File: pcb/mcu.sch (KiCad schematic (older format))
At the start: 24 parts, among them J1 Conn_01x04_Male, J2 Conn_01x04_Male, J3 Conn_01x03_Male, J4 Conn_01x03_Male, SW1 SW_Push, U1 STM32F103C8Tx, Y1 32.768KHz, Y2 8MHz

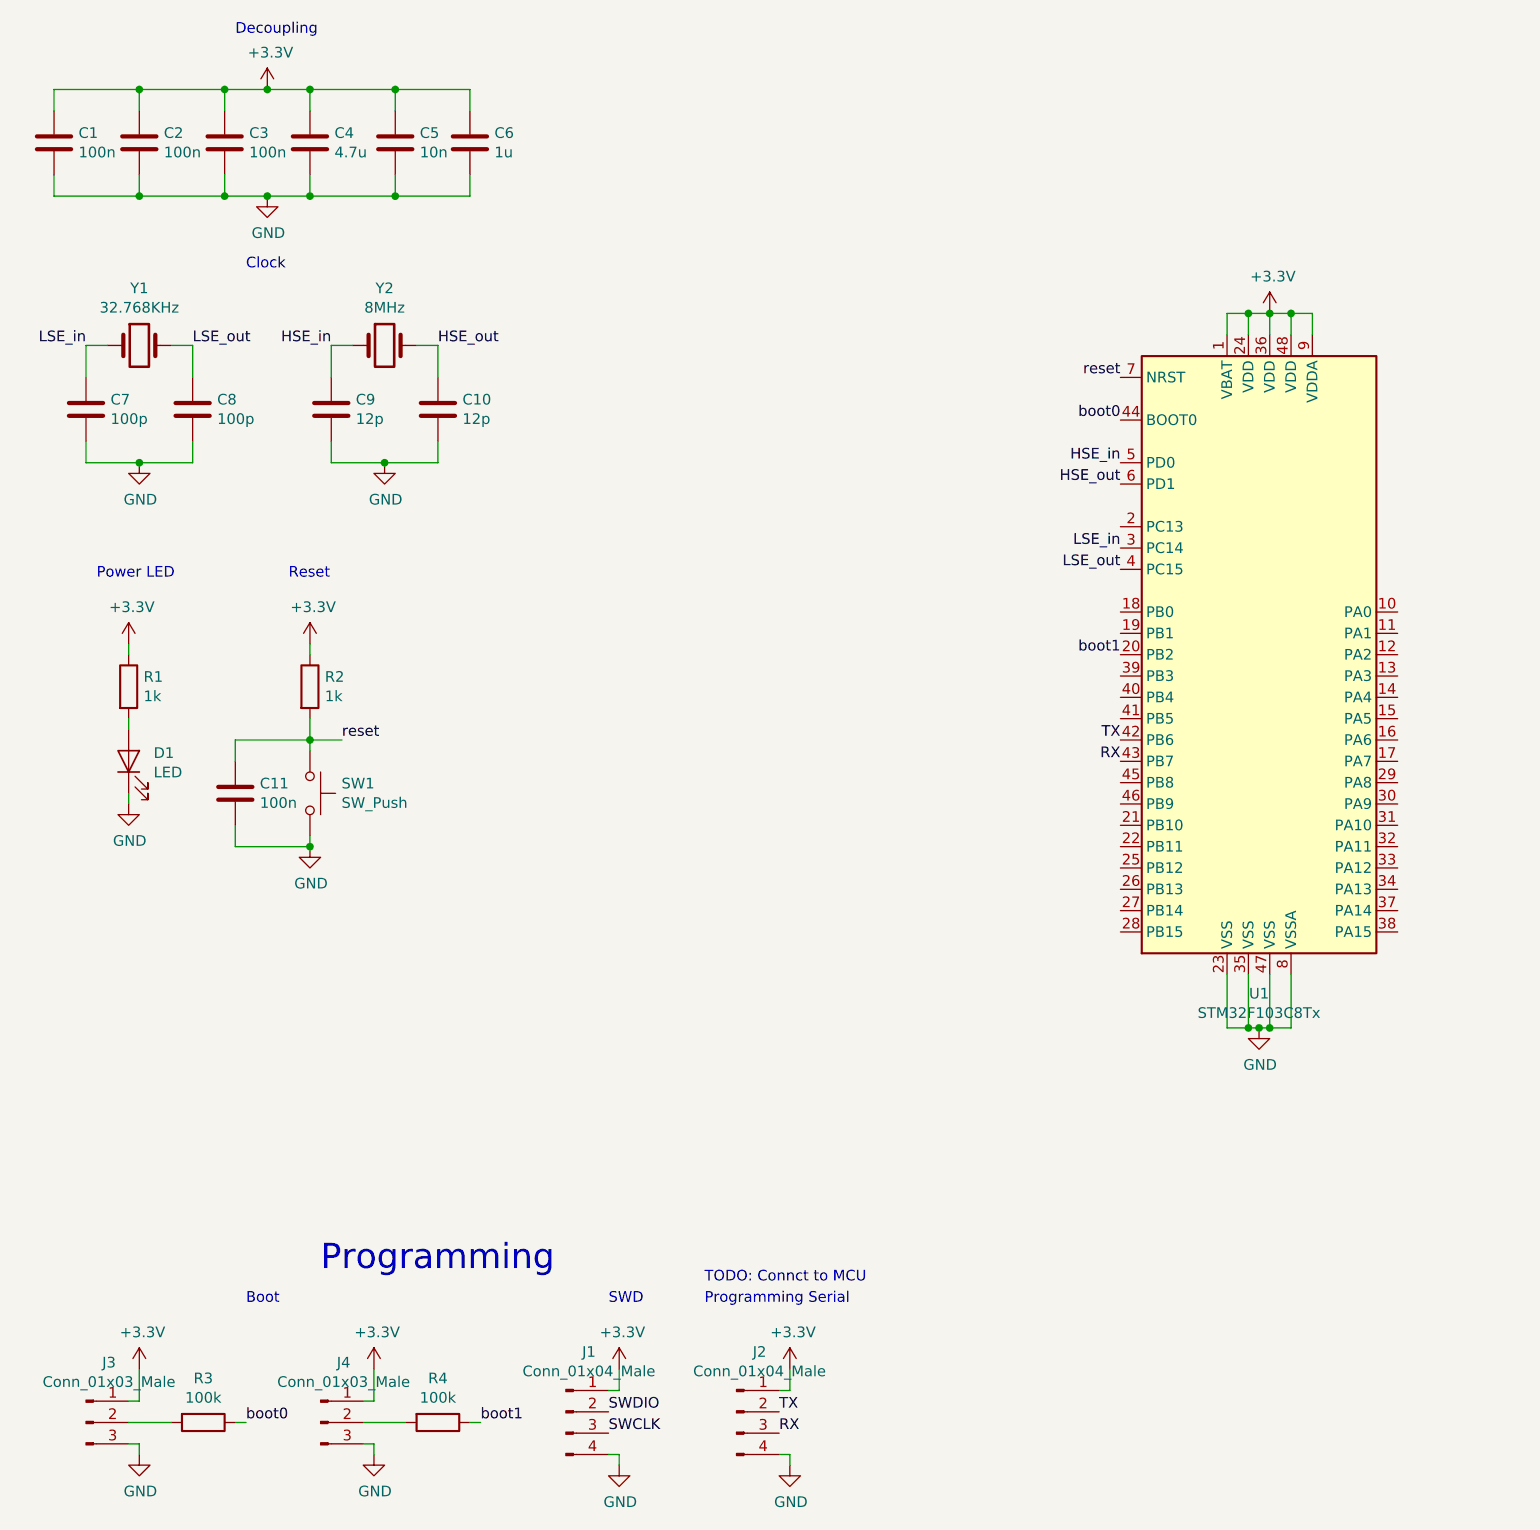
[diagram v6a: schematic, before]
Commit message: Use Buses for IR sensors
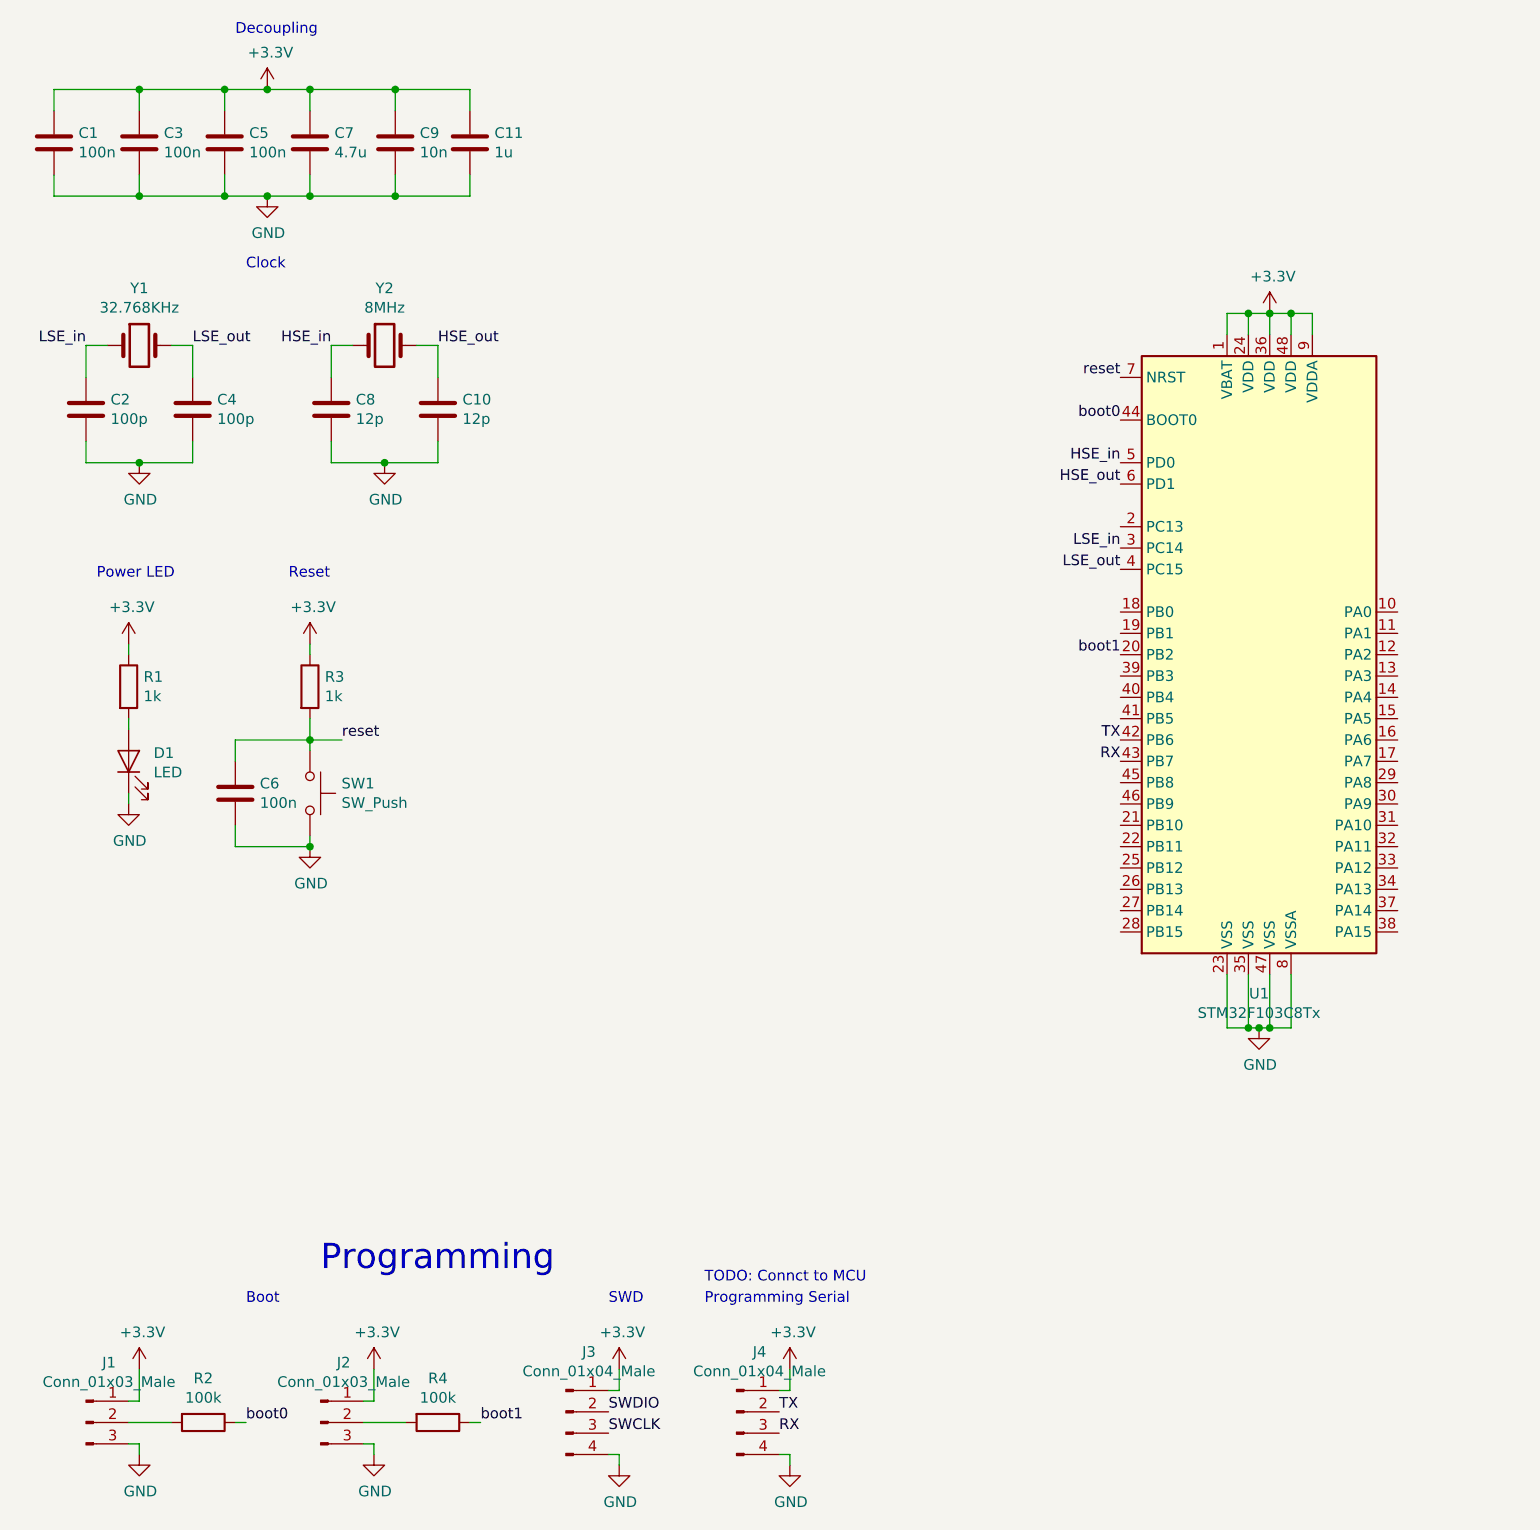
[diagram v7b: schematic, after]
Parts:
- renumbered C6 to C11, C7 to C2, C2 to C3, C8 to C4, C3 to C5, C11 to C6, C4 to C7, C9 to C8, C5 to C9, J3 to J1, J4 to J2, J1 to J3, J2 to J4, R3 to R2, R2 to R3
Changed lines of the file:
@@
 $Descr A4 11693 8268
 encoding utf-8
-Sheet 2 17
+Sheet 2 19
 Title ""
 Date ""
@@
 $EndComp
 $Comp
-L power:GND #PWR010
+L power:GND #PWR017
 U 1 1 5D0B3E48
 P 6300 5250
-F 0 "#PWR010" H 6300 5000 50  0001 C CNN
+F 0 "#PWR017" H 6300 5000 50  0001 C CNN
 F 1 "GND" H 6305 5077 50  0000 C CNN
 F 2 "" H 6300 5250 50  0001 C CNN
@@
 Decoupling
 $Comp
-L power:+3.3V #PWR01
+L power:+3.3V #PWR06
 U 1 1 5D0BC77C
 P 1650 850
-F 0 "#PWR01" H 1650 700 50  0001 C CNN
+F 0 "#PWR06" H 1650 700 50  0001 C CNN
 F 1 "+3.3V" H 1665 1023 50  0000 C CNN
 F 2 "" H 1650 850 50  0001 C CNN
@@
 $EndComp
 $Comp
-L Device:C C2
+L Device:C C3
 U 1 1 5D0BD12F
 P 1050 1100
-F 0 "C2" H 1165 1146 50  0000 L CNN
+F 0 "C3" H 1165 1146 50  0000 L CNN
 F 1 "100n" H 1165 1055 50  0000 L CNN
 F 2 "Capacitor_SMD:C_0805_2012Metric" H 1088 950 50  0001 C CNN
@@
 $EndComp
 $Comp
-L Device:C C3
+L Device:C C5
 U 1 1 5D0BD74C
 P 1450 1100
-F 0 "C3" H 1565 1146 50  0000 L CNN
+F 0 "C5" H 1565 1146 50  0000 L CNN
 F 1 "100n" H 1565 1055 50  0000 L CNN
 F 2 "Capacitor_SMD:C_0805_2012Metric" H 1488 950 50  0001 C CNN
@@
 	6350 1900 6250 1900
 $Comp
-L power:+3.3V #PWR03
+L power:+3.3V #PWR018
 U 1 1 5D0AFF21
 P 6350 1900
-F 0 "#PWR03" H 6350 1750 50  0001 C CNN
+F 0 "#PWR018" H 6350 1750 50  0001 C CNN
 F 1 "+3.3V" H 6365 2073 50  0000 C CNN
 F 2 "" H 6350 1900 50  0001 C CNN
@@
 	6300 5250 6250 5250
 $Comp
-L Device:C C4
+L Device:C C7
 U 1 1 5D0C6E4D
 P 1850 1100
-F 0 "C4" H 1965 1146 50  0000 L CNN
+F 0 "C7" H 1965 1146 50  0000 L CNN
 F 1 "4.7u" H 1965 1055 50  0000 L CNN
 F 2 "Capacitor_SMD:C_0805_2012Metric" H 1888 950 50  0001 C CNN
@@
 $EndComp
 $Comp
-L Device:C C5
+L Device:C C9
 U 1 1 5D0C8182
 P 2250 1100
-F 0 "C5" H 2365 1146 50  0000 L CNN
+F 0 "C9" H 2365 1146 50  0000 L CNN
 F 1 "10n" H 2365 1055 50  0000 L CNN
 F 2 "Capacitor_SMD:C_0805_2012Metric" H 2288 950 50  0001 C CNN
@@
 $EndComp
 $Comp
-L Device:C C6
+L Device:C C11
 U 1 1 5D0C8C05
 P 2600 1100
-F 0 "C6" H 2715 1146 50  0000 L CNN
+F 0 "C11" H 2715 1146 50  0000 L CNN
 F 1 "1u" H 2715 1055 50  0000 L CNN
 F 2 "Capacitor_SMD:C_0805_2012Metric" H 2638 950 50  0001 C CNN
@@
 	2250 850  1850 850
 $Comp
-L power:GND #PWR02
+L power:GND #PWR07
 U 1 1 5D0D37FC
 P 1650 1350
-F 0 "#PWR02" H 1650 1100 50  0001 C CNN
+F 0 "#PWR07" H 1650 1100 50  0001 C CNN
 F 1 "GND" H 1655 1177 50  0000 C CNN
 F 2 "" H 1650 1350 50  0001 C CNN
@@
 $EndComp
 $Comp
-L power:GND #PWR04
+L power:GND #PWR03
 U 1 1 5D0DEFF9
 P 1050 2600
-F 0 "#PWR04" H 1050 2350 50  0001 C CNN
+F 0 "#PWR03" H 1050 2350 50  0001 C CNN
 F 1 "GND" H 1055 2427 50  0000 C CNN
 F 2 "" H 1050 2600 50  0001 C CNN
@@
 $EndComp
 $Comp
-L Device:C C7
+L Device:C C2
 U 1 1 5D0DF7DE
 P 800 2350
-F 0 "C7" H 915 2396 50  0000 L CNN
+F 0 "C2" H 915 2396 50  0000 L CNN
 F 1 "100p" H 915 2305 50  0000 L CNN
 F 2 "Capacitor_SMD:C_0805_2012Metric" H 838 2200 50  0001 C CNN
@@
 $EndComp
 $Comp
-L Device:C C8
+L Device:C C4
 U 1 1 5D0DFE7A
 P 1300 2350
-F 0 "C8" H 1415 2396 50  0000 L CNN
+F 0 "C4" H 1415 2396 50  0000 L CNN
 F 1 "100p" H 1415 2305 50  0000 L CNN
 F 2 "Capacitor_SMD:C_0805_2012Metric" H 1338 2200 50  0001 C CNN
@@
 	1850 4400 1850 4350
 $Comp
-L Device:R R2
+L Device:R R3
 U 1 1 5D0DFE4B
 P 1850 3650
-F 0 "R2" H 1920 3696 50  0000 L CNN
+F 0 "R3" H 1920 3696 50  0000 L CNN
 F 1 "1k" H 1920 3605 50  0000 L CNN
 F 2 "Resistor_SMD:R_0805_2012Metric" V 1780 3650 50  0001 C CNN
@@
 	1850 3950 1850 3900
 $Comp
-L power:+3.3V #PWR07
+L power:+3.3V #PWR08
 U 1 1 5D0EA230
 P 1850 3450
-F 0 "#PWR07" H 1850 3300 50  0001 C CNN
+F 0 "#PWR08" H 1850 3300 50  0001 C CNN
 F 1 "+3.3V" H 1865 3623 50  0000 C CNN
 F 2 "" H 1850 3450 50  0001 C CNN
@@
 	1850 3450 1850 3500
 $Comp
-L Device:C C11
+L Device:C C6
 U 1 1 5D0EEFC1
 P 1500 4150
-F 0 "C11" H 1615 4196 50  0000 L CNN
+F 0 "C6" H 1615 4196 50  0000 L CNN
 F 1 "100n" H 1615 4105 50  0000 L CNN
 F 2 "Capacitor_SMD:C_0805_2012Metric" H 1538 4000 50  0001 C CNN
@@
 Boot\n
 $Comp
-L Connector:Conn_01x03_Male J3
+L Connector:Conn_01x03_Male J1
 U 1 1 5D0FA90C
 P 800 7100
-F 0 "J3" H 908 7381 50  0000 C CNN
+F 0 "J1" H 908 7381 50  0000 C CNN
 F 1 "Conn_01x03_Male" H 908 7290 50  0000 C CNN
 F 2 "Connector_PinHeader_2.54mm:PinHeader_1x03_P2.54mm_Vertical" H 800 7100 50  0001 C CNN
@@
 $EndComp
 $Comp
-L power:+3.3V #PWR011
+L power:+3.3V #PWR04
 U 1 1 5D0FB455
 P 1050 6850
-F 0 "#PWR011" H 1050 6700 50  0001 C CNN
+F 0 "#PWR04" H 1050 6700 50  0001 C CNN
 F 1 "+3.3V" H 1065 7023 50  0000 C CNN
 F 2 "" H 1050 6850 50  0001 C CNN
@@
 	1050 7000 1000 7000
 $Comp
-L power:GND #PWR015
+L power:GND #PWR05
 U 1 1 5D0FD013
 P 1050 7250
-F 0 "#PWR015" H 1050 7000 50  0001 C CNN
+F 0 "#PWR05" H 1050 7000 50  0001 C CNN
 F 1 "GND" H 1055 7077 50  0000 C CNN
 F 2 "" H 1050 7250 50  0001 C CNN
@@
 	3300 7300 3300 7250
 $Comp
-L power:GND #PWR017
+L power:GND #PWR014
 U 1 1 5D0B3FE0
 P 3300 7300
-F 0 "#PWR017" H 3300 7050 50  0001 C CNN
+F 0 "#PWR014" H 3300 7050 50  0001 C CNN
 F 1 "GND" H 3305 7127 50  0000 C CNN
 F 2 "" H 3300 7300 50  0001 C CNN
@@
 $EndComp
 $Comp
-L Connector:Conn_01x04_Male J1
+L Connector:Conn_01x04_Male J3
 U 1 1 5D0B2068
 P 3050 7050
-F 0 "J1" H 3158 7331 50  0000 C CNN
+F 0 "J3" H 3158 7331 50  0000 C CNN
 F 1 "Conn_01x04_Male" H 3158 7240 50  0000 C CNN
 F 2 "Connector_PinHeader_2.54mm:PinHeader_1x04_P2.54mm_Vertical" H 3050 7050 50  0001 C CNN
@@
 $EndComp
 $Comp
-L Device:R R3
+L Device:R R2
 U 1 1 5D116F8B
 P 1350 7100
-F 0 "R3" V 1143 7100 50  0000 C CNN
+F 0 "R2" V 1143 7100 50  0000 C CNN
 F 1 "100k" V 1234 7100 50  0000 C CNN
 F 2 "Resistor_SMD:R_0805_2012Metric" V 1280 7100 50  0001 C CNN
@@
 $EndComp
 $Comp
-L power:+3.3V #PWR06
+L power:+3.3V #PWR01
 U 1 1 5D122362
 P 1000 3450
-F 0 "#PWR06" H 1000 3300 50  0001 C CNN
+F 0 "#PWR01" H 1000 3300 50  0001 C CNN
 F 1 "+3.3V" H 1015 3623 50  0000 C CNN
 F 2 "" H 1000 3450 50  0001 C CNN
@@
 	1000 3800 1000 3850
 $Comp
-L power:GND #PWR08
+L power:GND #PWR02
 U 1 1 5D1254B3
 P 1000 4200
-F 0 "#PWR08" H 1000 3950 50  0001 C CNN
+F 0 "#PWR02" H 1000 3950 50  0001 C CNN
 F 1 "GND" H 1005 4027 50  0000 C CNN
 F 2 "" H 1000 4200 50  0001 C CNN
@@
 Power LED
 $Comp
-L Connector:Conn_01x03_Male J4
+L Connector:Conn_01x03_Male J2
 U 1 1 5D159F2F
 P 1900 7100
-F 0 "J4" H 2008 7381 50  0000 C CNN
+F 0 "J2" H 2008 7381 50  0000 C CNN
 F 1 "Conn_01x03_Male" H 2008 7290 50  0000 C CNN
 F 2 "Connector_PinHeader_2.54mm:PinHeader_1x03_P2.54mm_Vertical" H 1900 7100 50  0001 C CNN
@@
 $EndComp
 $Comp
-L power:+3.3V #PWR012
+L power:+3.3V #PWR010
 U 1 1 5D159F35
 P 2150 6850
-F 0 "#PWR012" H 2150 6700 50  0001 C CNN
+F 0 "#PWR010" H 2150 6700 50  0001 C CNN
 F 1 "+3.3V" H 2165 7023 50  0000 C CNN
 F 2 "" H 2150 6850 50  0001 C CNN
@@
 	2150 7000 2100 7000
 $Comp
-L power:GND #PWR016
+L power:GND #PWR011
 U 1 1 5D159F3D
 P 2150 7250
-F 0 "#PWR016" H 2150 7000 50  0001 C CNN
+F 0 "#PWR011" H 2150 7000 50  0001 C CNN
 F 1 "GND" H 2155 7077 50  0000 C CNN
 F 2 "" H 2150 7250 50  0001 C CNN
@@
 $EndComp
 $Comp
-L power:GND #PWR05
+L power:GND #PWR012
 U 1 1 5D1B0C86
 P 2200 2600
-F 0 "#PWR05" H 2200 2350 50  0001 C CNN
+F 0 "#PWR012" H 2200 2350 50  0001 C CNN
 F 1 "GND" H 2205 2427 50  0000 C CNN
 F 2 "" H 2200 2600 50  0001 C CNN
@@
 $EndComp
 $Comp
-L Device:C C9
+L Device:C C8
 U 1 1 5D1B0C8C
 P 1950 2350
-F 0 "C9" H 2065 2396 50  0000 L CNN
+F 0 "C8" H 2065 2396 50  0000 L CNN
 F 1 "12p" H 2065 2305 50  0000 L CNN
 F 2 "Capacitor_SMD:C_0805_2012Metric" H 1988 2200 50  0001 C CNN
@@
 	4100 6850 4100 6950
 $Comp
-L power:+3.3V #PWR014
+L power:+3.3V #PWR015
 U 1 1 5D621CD5
 P 4100 6850
-F 0 "#PWR014" H 4100 6700 50  0001 C CNN
+F 0 "#PWR015" H 4100 6700 50  0001 C CNN
 F 1 "+3.3V" H 4115 7023 50  0000 C CNN
 F 2 "" H 4100 6850 50  0001 C CNN
@@
 	4100 7300 4100 7250
 $Comp
-L power:GND #PWR018
+L power:GND #PWR016
 U 1 1 5D621CDD
 P 4100 7300
-F 0 "#PWR018" H 4100 7050 50  0001 C CNN
+F 0 "#PWR016" H 4100 7050 50  0001 C CNN
 F 1 "GND" H 4105 7127 50  0000 C CNN
 F 2 "" H 4100 7300 50  0001 C CNN
@@
 $EndComp
 $Comp
-L Connector:Conn_01x04_Male J2
+L Connector:Conn_01x04_Male J4
 U 1 1 5D621CE3
 P 3850 7050
-F 0 "J2" H 3958 7331 50  0000 C CNN
+F 0 "J4" H 3958 7331 50  0000 C CNN
 F 1 "Conn_01x04_Male" H 3958 7240 50  0000 C CNN
 F 2 "Connector_PinHeader_2.54mm:PinHeader_1x04_P2.54mm_Vertical" H 3850 7050 50  0001 C CNN
